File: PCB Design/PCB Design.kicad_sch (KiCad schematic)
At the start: 0 parts

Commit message: intial circuit implementation
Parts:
- added D1, D2, D3: LED, LED_THT:LED_D3.0mm, symbol Device:LED
- added J1: Conn_01x02_Pin, Connector_Wire:SolderWire-1sqmm_1x02_P5.4mm_D1.4mm_OD2.7mm, symbol Connector:Conn_01x02_Pin
- added R1: 35, Resistor_THT:R_Axial_DIN0207_L6.3mm_D2.5mm_P10.16mm_Horizontal, symbol Device:R
- added SW1: SW_SP3T, Button_Switch_THT:SW_DIP_SPSTx02_Piano_10.8x6.64mm_W7.62mm_P2.54mm, symbol Switch:SW_SP3T
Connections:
- new net: J1.1 (Pin_1), R1.1
- new net: R1.2, SW1.3
- new net: D1.1 (K), D2.1 (K), D3.1 (K), J1.2 (Pin_2)
- new net: D2.2 (A), SW1.2
- new net: D3.2 (A), SW1.1
- new net: D1.2 (A), SW1.4

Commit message: adjustements the PCB schematic
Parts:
- removed J1: Conn_01x02_Pin, Connector_Wire:SolderWire-1sqmm_1x02_P5.4mm_D1.4mm_OD2.7mm, symbol Connector:Conn_01x02_Pin
- added D4, D5: LED, LED_THT:LED_D3.0mm, symbol Device:LED
- added J1, J10, J11, J2, J3, J4, J5, J6, J7, J8, J9: Conn_01x01_Pin, Connector_Wire:SolderWire-1sqmm_1x01_D1.4mm_OD2.7mm, symbol Connector:Conn_01x01_Pin
- added R2, R3: 35, Resistor_THT:R_Axial_DIN0207_L6.3mm_D2.5mm_P10.16mm_Horizontal, symbol Device:R
- added SW2: SW_DPST_x2, symbol Switch:SW_DPST_x2
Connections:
- net at R1.1: now also J1.1 (Pin_1)
- new net: D3.1 (K), J4.1 (Pin_1)
- new net: J9.1 (Pin_1), R3.2
- new net: D2.1 (K), J3.1 (Pin_1)
- new net: J10.1 (Pin_1), R2.2
- new net: J7.1 (Pin_1), SW2.4 (B)
- new net: J8.1 (Pin_1), SW2.2 (B)
- new net: D4.1 (K), D5.1 (K), J11.1 (Pin_1)
- new net: D4.2 (A), R2.1
- new net: D5.2 (A), R3.1
- new net: J5.1 (Pin_1), SW2.1 (A)
- new net: D1.1 (K), J2.1 (Pin_1)
- new net: J6.1 (Pin_1), SW2.3 (A)

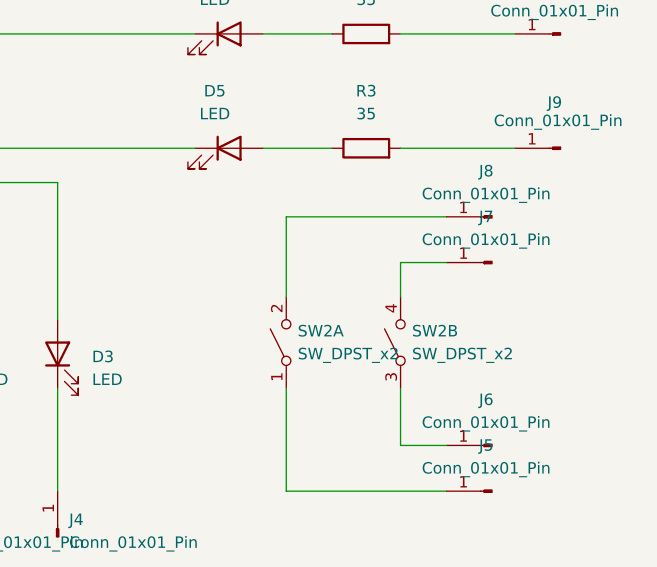
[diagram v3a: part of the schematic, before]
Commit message: intial pcb desin and testing of 3d model - some contraint voilations
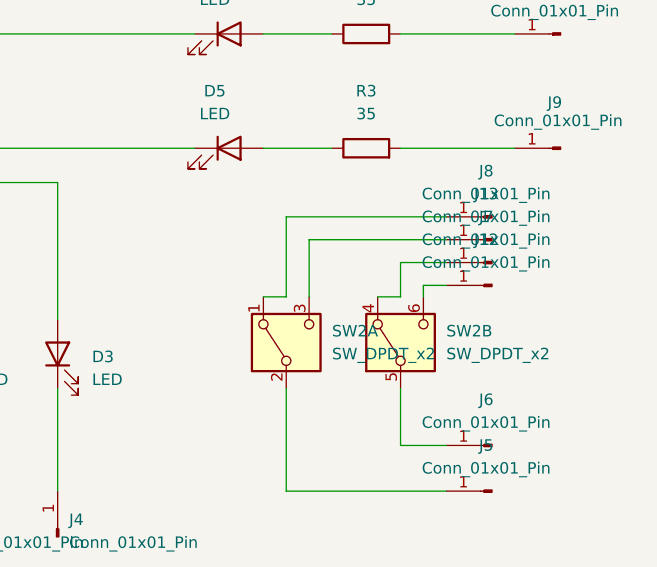
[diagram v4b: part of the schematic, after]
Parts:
- removed SW2: SW_DPST_x2, symbol Switch:SW_DPST_x2
- added J12, J13: Conn_01x01_Pin, Connector_Wire:SolderWire-1sqmm_1x01_D1.4mm_OD2.7mm, symbol Connector:Conn_01x01_Pin
- added SW2: SW_DPDT_x2, Button_Switch_THT:SW_CK_JS202011CQN_DPDT_Straight, symbol Switch:SW_DPDT_x2
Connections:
- net at J7.1 (Pin_1): now also SW2.4 (A)
- net at J8.1 (Pin_1): now also SW2.1 (A)
- net at J5.1 (Pin_1): now also SW2.2 (B)
- net at J6.1 (Pin_1): now also SW2.5 (B)
- new net: J13.1 (Pin_1), SW2.3 (C)
- new net: J12.1 (Pin_1), SW2.6 (C)

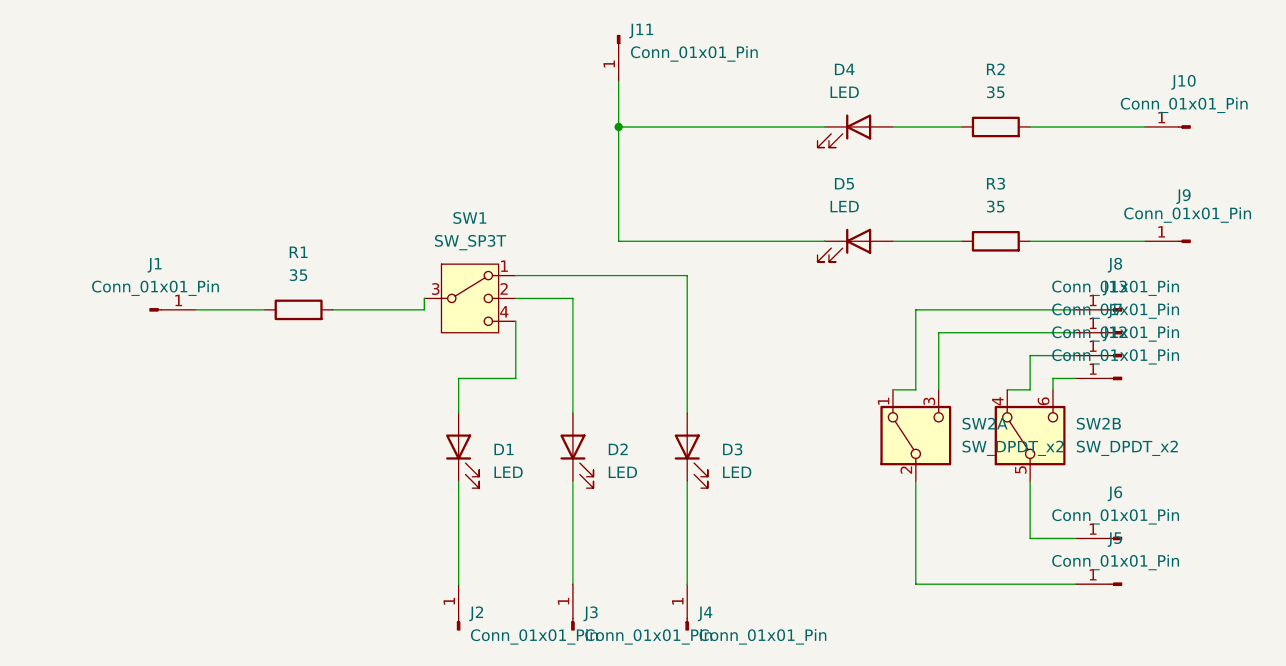
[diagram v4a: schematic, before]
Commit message: altered schematic and PCB layout for new SPDT switches
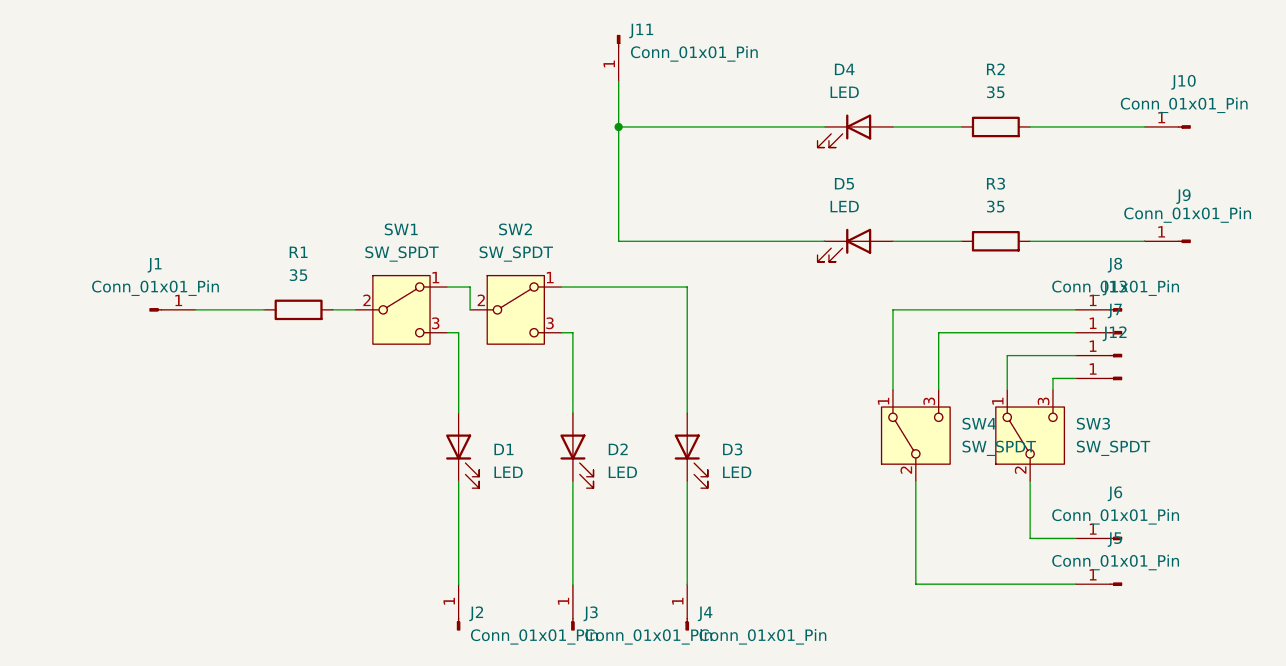
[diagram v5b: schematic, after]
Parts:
- removed SW1: SW_SP3T, Button_Switch_THT:SW_DIP_SPSTx02_Piano_10.8x6.64mm_W7.62mm_P2.54mm, symbol Switch:SW_SP3T
- removed SW2: SW_DPDT_x2, Button_Switch_THT:SW_CK_JS202011CQN_DPDT_Straight, symbol Switch:SW_DPDT_x2
- added SW1, SW2, SW3, SW4: SW_SPDT, symbol Switch:SW_SPDT
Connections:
- net at R1.2: now also SW1.2 (B)
- net at J8.1 (Pin_1): now also SW4.1 (A)
- net at J5.1 (Pin_1): now also SW4.2 (B)
- net at J13.1 (Pin_1): now also SW4.3 (C)
- net at J7.1 (Pin_1): now also SW3.1 (A)
- net at J6.1 (Pin_1): now also SW3.2 (B)
- net at J12.1 (Pin_1): now also SW3.3 (C)
- net at D2.2 (A): now also SW2.3 (C)
- net at D3.2 (A): now also SW2.1 (A)
- net at D1.2 (A): now also SW1.3 (C)
- new net: SW1.1 (A), SW2.2 (B)

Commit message: adding footprint for the swithces
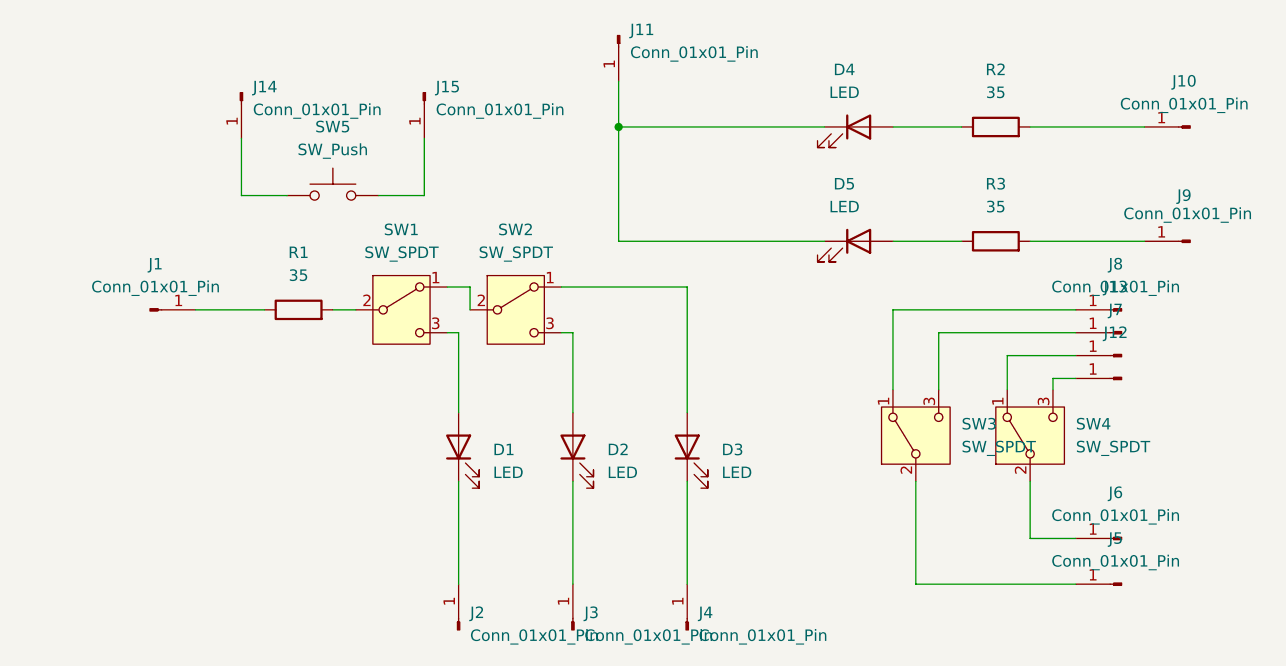
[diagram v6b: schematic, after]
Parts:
- removed SW1, SW2, SW3, SW4: SW_SPDT, symbol Switch:SW_SPDT
- added J14, J15: Conn_01x01_Pin, Connector_Wire:SolderWire-1sqmm_1x01_D1.4mm_OD2.7mm, symbol Connector:Conn_01x01_Pin
- added SW1, SW2, SW3, SW4: SW_SPDT, footprints :SW_SPDT, symbol SPDT_footprint:SW_SPDT
- added SW5: SW_Push, symbol Switch:SW_Push
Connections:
- net at R1.2: now also SW1.2 (B)
- net at J7.1 (Pin_1): now also SW4.1 (A)
- net at J6.1 (Pin_1): now also SW4.2 (B)
- net at J12.1 (Pin_1): now also SW4.3 (C)
- net at J13.1 (Pin_1): now also SW3.3 (C)
- net at D2.2 (A): now also SW2.3 (C)
- net at D1.2 (A): now also SW1.3 (C)
- net at J8.1 (Pin_1): now also SW3.1 (A)
- net at J5.1 (Pin_1): now also SW3.2 (B)
- net at D3.2 (A): now also SW2.1 (A)
- new net: SW1.1 (A), SW2.2 (B)
- new net: J14.1 (Pin_1), SW5.1
- new net: J15.1 (Pin_1), SW5.2

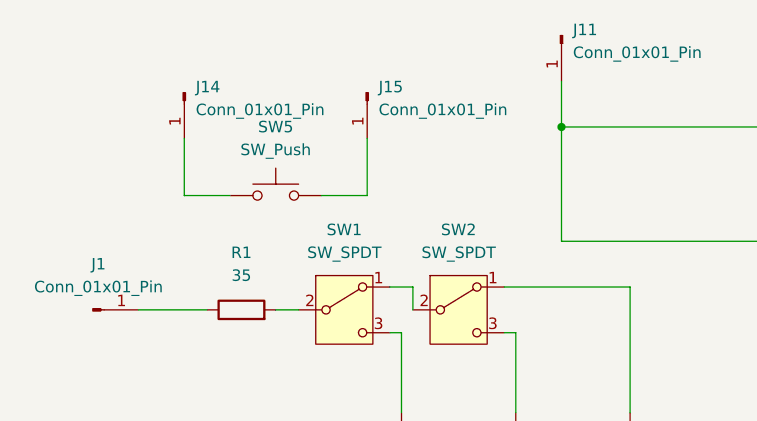
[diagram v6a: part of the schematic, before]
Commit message: completed main pcb design
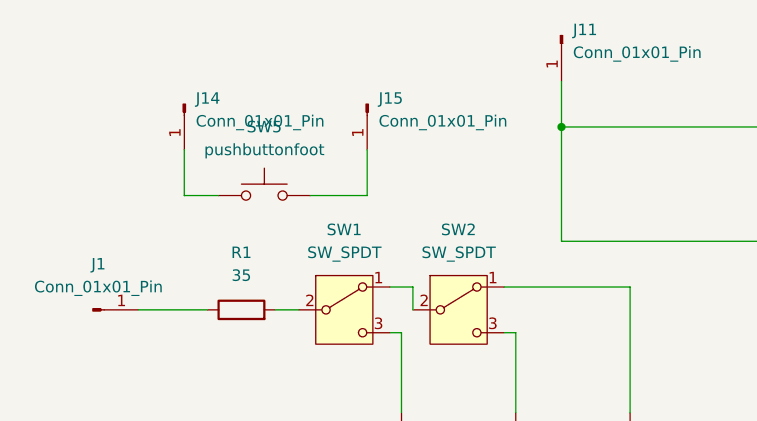
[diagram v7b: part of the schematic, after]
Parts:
- removed SW5: SW_Push, symbol Switch:SW_Push
- added SW5: pushbuttonfoot, buttonfootprint:Untitled, symbol button_footprint:pushbuttonfoot
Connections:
- net at J14.1 (Pin_1): now also SW5.1
- net at J15.1 (Pin_1): now also SW5.2
